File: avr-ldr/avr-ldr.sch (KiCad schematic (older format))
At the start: 23 parts, among them CON1 AVR-ISP-6, IC1 ATTINY2313-P, P1 RJ11, P2 CONN_01X05, U1 PCA82C250, Y1 4MHz

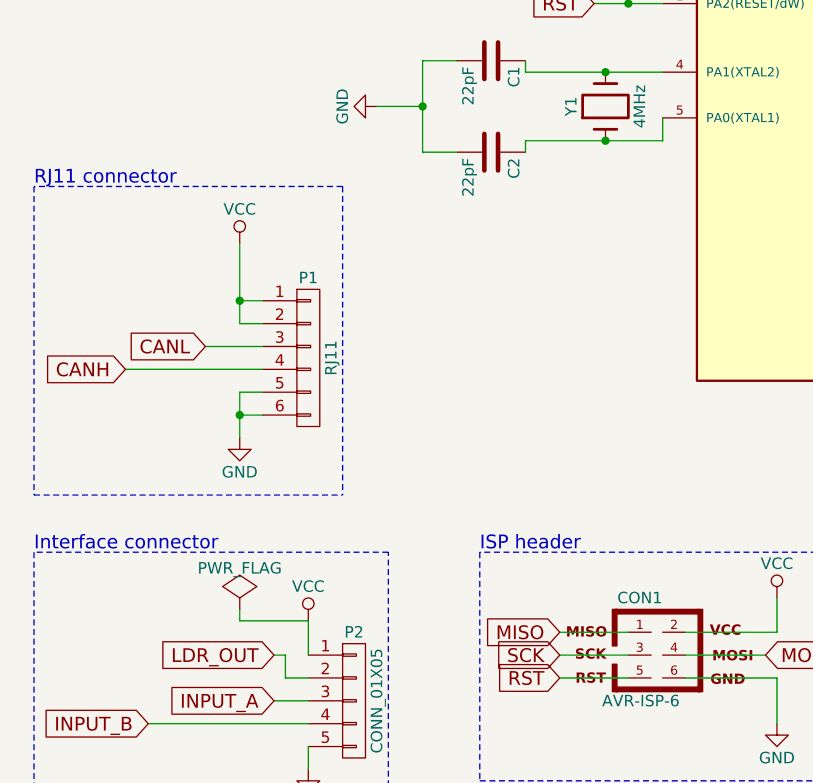
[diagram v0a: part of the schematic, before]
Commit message: Add ferrite beads and correctly hook up the power flag
It'll enter from the RJ-11 connector.
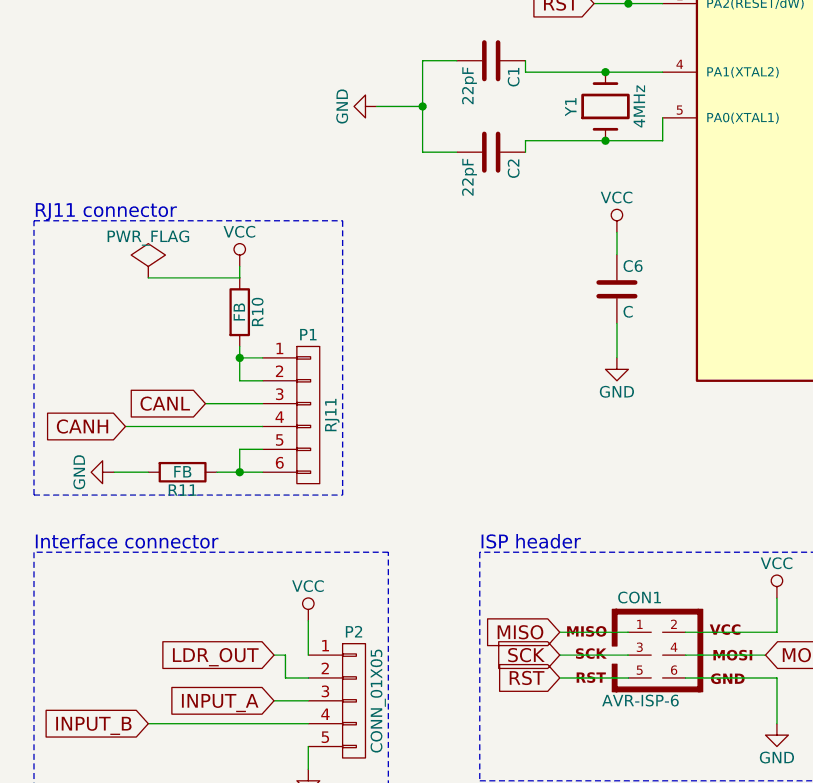
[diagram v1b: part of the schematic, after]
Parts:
- added C6: C, symbol C
- added R10, R11: FB, symbol R
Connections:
- net GND: now also C6.2, R11.2; no longer P1.5 (P5), P1.6 (P6)
- net VCC: now also C6.1, R10.1; no longer P1.1 (P1), P1.2 (P2)
- new net: P1.1 (P1), P1.2 (P2), R10.2
- new net: P1.5 (P5), P1.6 (P6), R11.1
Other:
- moved on the sheet: P1

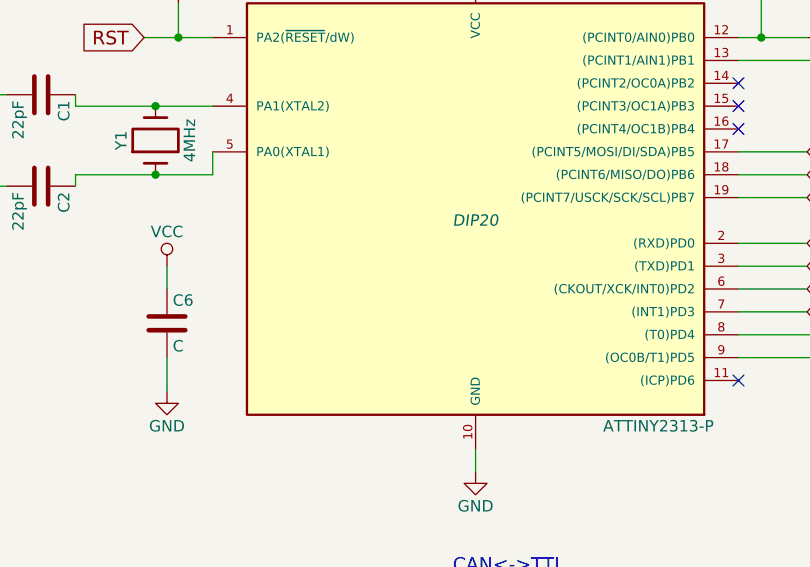
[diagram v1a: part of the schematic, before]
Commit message: First attempt at PCB layout
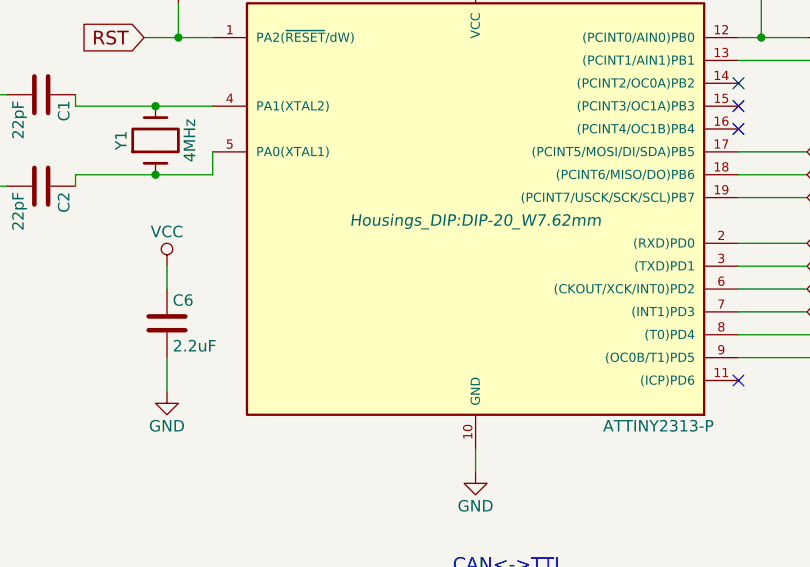
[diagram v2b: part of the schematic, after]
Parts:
- C1, C2, C3, C4, C5: footprint (none) -> Capacitors_SMD:C_0603
- C6: value C -> 2.2uF; footprint (none) -> Capacitors_SMD:C_0603
- CON1: footprint AVR-ISP-6 -> Pin_Headers:Pin_Header_Straight_2x03
- D1, D2: footprint (none) -> LEDs:LED_0603
- IC1: footprint DIP20 -> Housings_DIP:DIP-20_W7.62mm
- P1: footprint (none) -> SparkFun-Connectors:RJ11-6
- P2: footprint (none) -> Pin_Headers:Pin_Header_Straight_1x05
- R1, R10, R11, R2, R3, R4, R5, R6, R7, R8, R9: footprint (none) -> Resistors_SMD:R_0603
- RV1: footprint (none) -> Potentiometers:Potentiometer_Triwood_RM-065
- U1: footprint (none) -> Housings_SOIC:SOIC-8_3.9x4.9mm_Pitch1.27mm
- Y1: footprint (none) -> Crystals:Crystal_HC49-U_Vertical
